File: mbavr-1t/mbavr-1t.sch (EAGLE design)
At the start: 9 parts

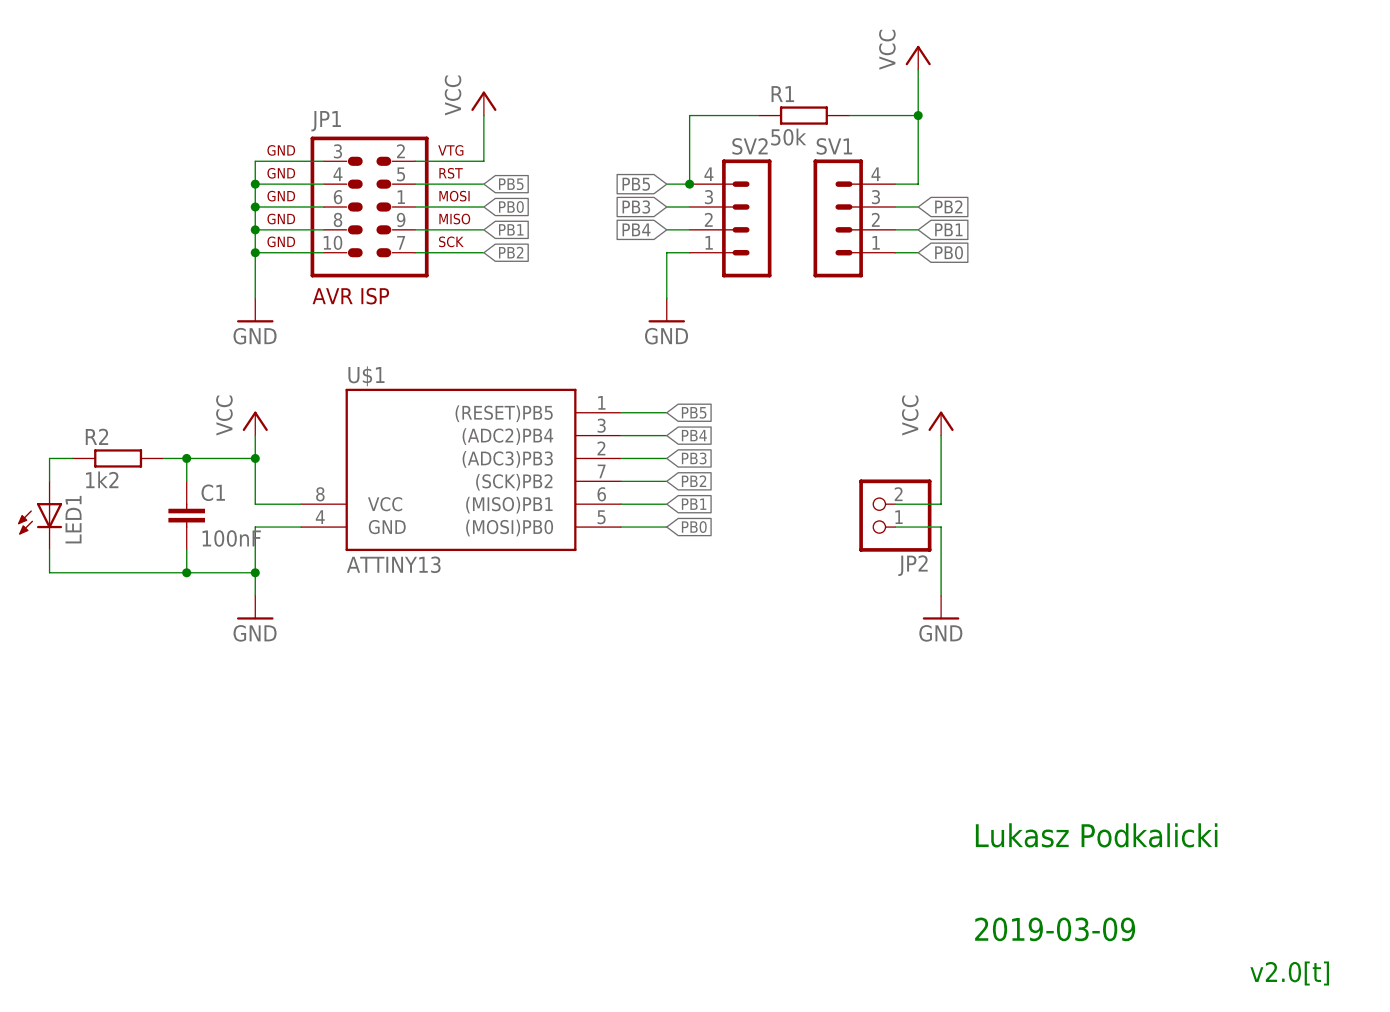
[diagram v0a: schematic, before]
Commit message: Update R2 value.
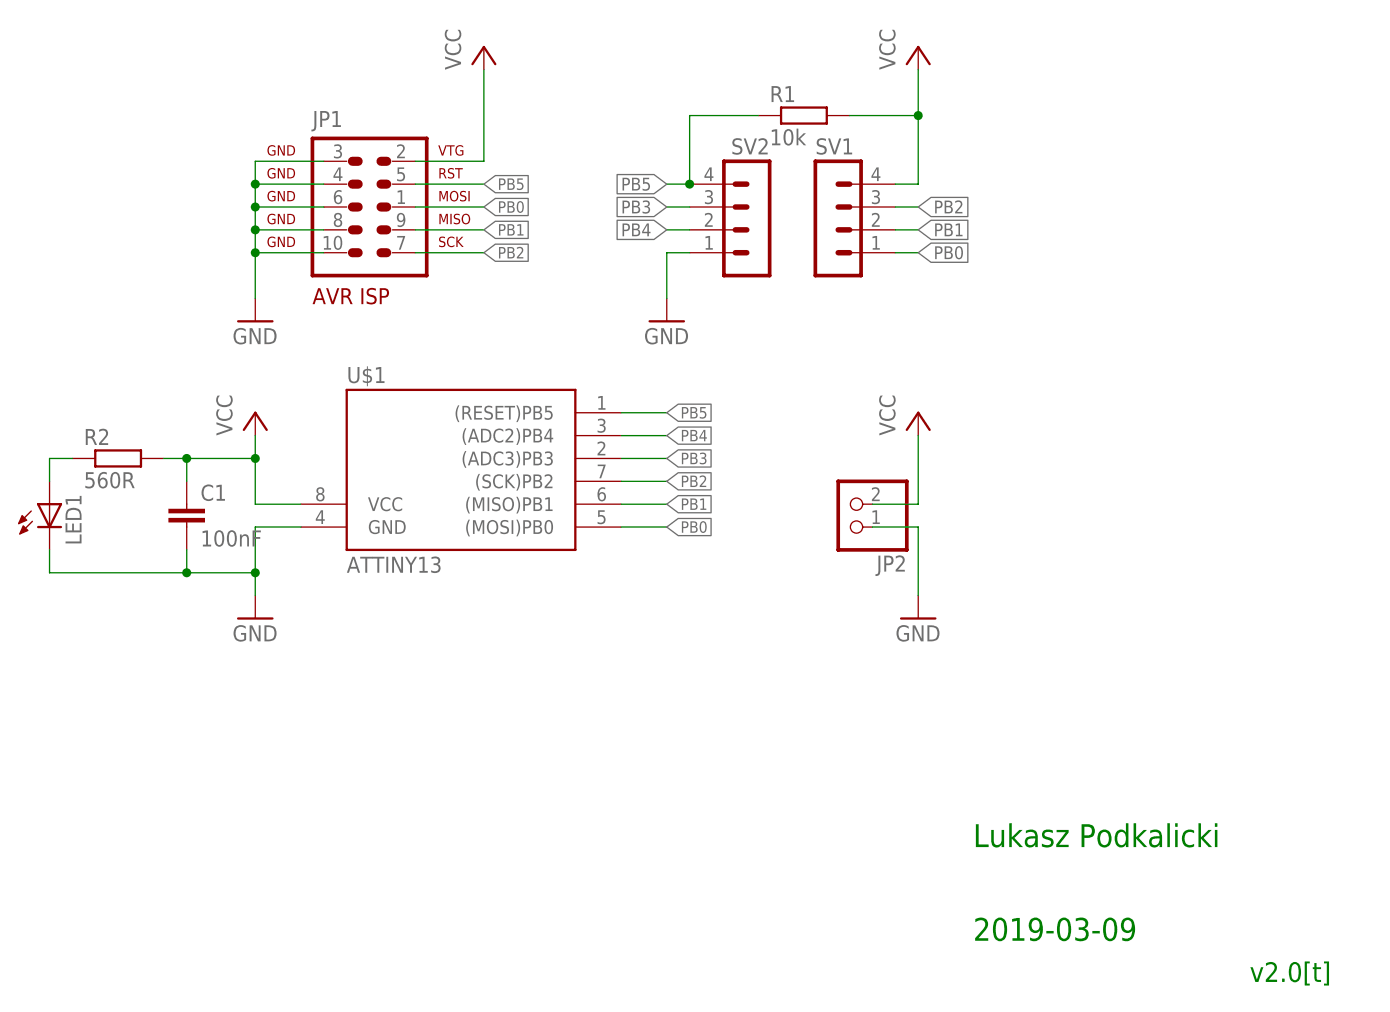
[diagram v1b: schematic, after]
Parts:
- R1: value 50k -> 10k
- R2: value 1k2 -> 560R
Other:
- moved on the sheet: JP2
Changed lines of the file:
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@@
 <part name="FRAME1" library="frames" deviceset="DINA5_L" device=""/>
 <part name="C1" library="rcl" deviceset="C-EU" device="C1206K" value="100nF"/>
-<part name="R1" library="resistor" deviceset="R-EU_" device="R1206" value="50k"/>
-<part name="R2" library="resistor" deviceset="R-EU_" device="R1206" value="1k2"/>
+<part name="R1" library="resistor" deviceset="R-EU_" device="R1206" value="10k"/>
+<part name="R2" library="resistor" deviceset="R-EU_" device="R1206" value="560R"/>
 <part name="LED1" library="led" deviceset="LED" device="SML1206"/>
 </parts>
@@
 <instance part="JP1" gate="G$1" x="5.08" y="86.36"/>
 <instance part="GND2" gate="1" x="-7.62" y="73.66"/>
-<instance part="P+2" gate="VCC" x="17.78" y="99.06"/>
+<instance part="P+2" gate="VCC" x="17.78" y="104.14"/>
 <instance part="SV1" gate="1" x="55.88" y="86.36"/>
 <instance part="SV2" gate="1" x="48.26" y="86.36" rot="MR0"/>
 <instance part="GND3" gate="1" x="38.1" y="73.66"/>
 <instance part="P+3" gate="VCC" x="66.04" y="104.14"/>
-<instance part="JP2" gate="G$1" x="60.96" y="53.34" rot="R180"/>
-<instance part="GND4" gate="1" x="68.58" y="40.64"/>
-<instance part="P+4" gate="VCC" x="68.58" y="63.5"/>
+<instance part="JP2" gate="G$1" x="58.42" y="53.34" rot="R180"/>
+<instance part="GND4" gate="1" x="66.04" y="40.64"/>
+<instance part="P+4" gate="VCC" x="66.04" y="63.5"/>
 <instance part="FRAME1" gate="G$1" x="-68.58" y="-5.08" smashed="yes">
 <attribute name="DRAWING_NAME" x="72.39" y="10.16" size="2.54" layer="91" font="vector"/>
@@
 <segment>
 <pinref part="GND4" gate="1" pin="GND"/>
-<wire x1="68.58" y1="50.8" x2="68.58" y2="43.18" width="0.1524" layer="91"/>
+<wire x1="66.04" y1="50.8" x2="66.04" y2="43.18" width="0.1524" layer="91"/>
 <pinref part="JP2" gate="G$1" pin="1"/>
-<wire x1="68.58" y1="50.8" x2="63.5" y2="50.8" width="0.1524" layer="91"/>
+<wire x1="66.04" y1="50.8" x2="60.96" y2="50.8" width="0.1524" layer="91"/>
 </segment>
 </net>
@@
 <wire x1="10.16" y1="91.44" x2="17.78" y2="91.44" width="0.1524" layer="91"/>
 <pinref part="P+2" gate="VCC" pin="VCC"/>
-<wire x1="17.78" y1="91.44" x2="17.78" y2="96.52" width="0.1524" layer="91"/>
+<wire x1="17.78" y1="91.44" x2="17.78" y2="101.6" width="0.1524" layer="91"/>
 </segment>
 <segment>
@@
 <segment>
 <pinref part="P+4" gate="VCC" pin="VCC"/>
-<wire x1="68.58" y1="53.34" x2="68.58" y2="60.96" width="0.1524" layer="91"/>
+<wire x1="66.04" y1="53.34" x2="66.04" y2="60.96" width="0.1524" layer="91"/>
 <pinref part="JP2" gate="G$1" pin="2"/>
-<wire x1="63.5" y1="53.34" x2="68.58" y2="53.34" width="0.1524" layer="91"/>
+<wire x1="60.96" y1="53.34" x2="66.04" y2="53.34" width="0.1524" layer="91"/>
 </segment>
 </net>
